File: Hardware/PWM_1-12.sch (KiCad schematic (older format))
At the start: 6 parts, among them J1 GH-6, J2 GH-6, J3 GH-6, J4 GH-6, J5 GH-6, J6 GH-6

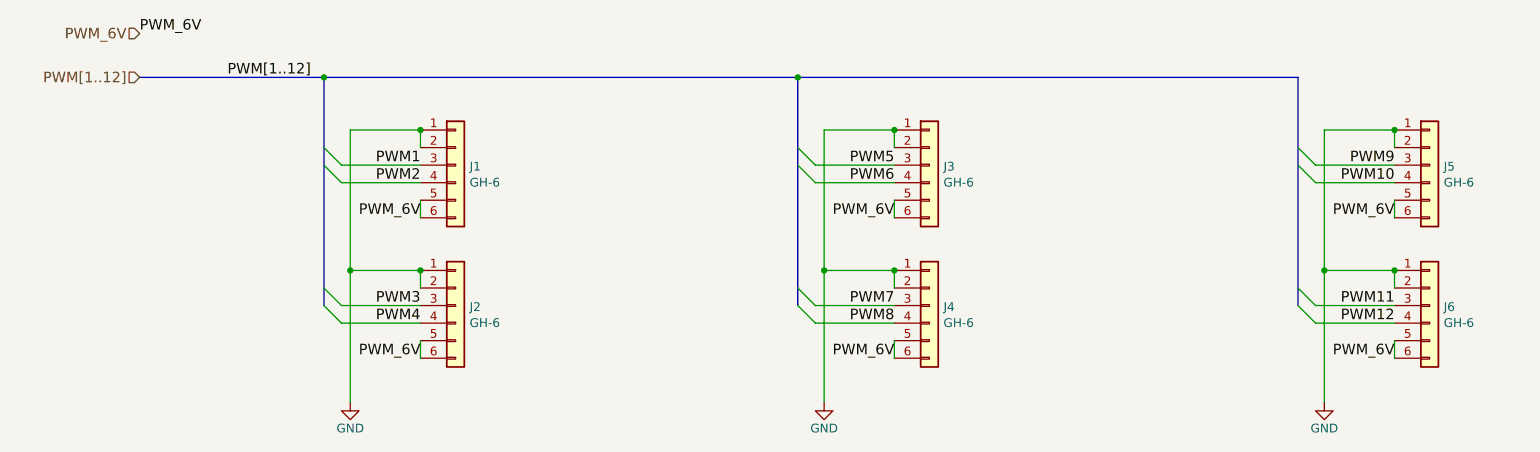
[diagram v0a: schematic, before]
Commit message: Added additional headers to some interfaces, GPIOs, and FTDI pins. Added silks
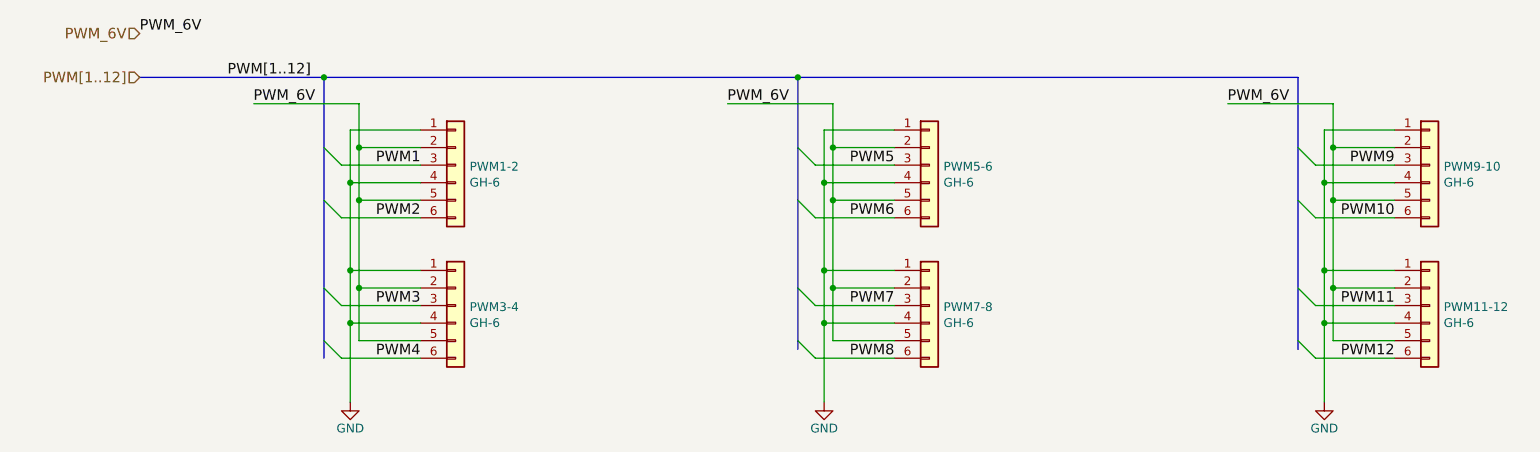
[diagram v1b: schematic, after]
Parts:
- PWM1-2: renamed from J1; part_num CONN-09 -> CONN-009
- PWM11-12: renamed from J6; part_num CONN-09 -> CONN-009
- PWM3-4: renamed from J2; part_num CONN-09 -> CONN-009
- PWM5-6: renamed from J3; part_num CONN-09 -> CONN-009
- PWM7-8: renamed from J4; part_num CONN-09 -> CONN-009
- PWM9-10: renamed from J5; part_num CONN-09 -> CONN-009
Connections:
- wire segments 36 -> 63
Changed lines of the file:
@@
 Text Label 2700 1400 2    60   ~ 0
 PWM1
-Text Label 2700 1500 2    60   ~ 0
+Text Label 2700 1700 2    60   ~ 0
 PWM2
 Text Label 2700 2200 2    60   ~ 0
 PWM3
-Text Label 2700 2300 2    60   ~ 0
+Text Label 2700 2500 2    60   ~ 0
 PWM4
 Text HLabel 1100 900  0    60   Input ~ 0
@@
 Text Label 1600 900  0    60   ~ 0
 PWM[1..12]
-Text Label 2700 2500 2    60   ~ 0
-PWM_6V
 Text Label 1100 650  0    60   ~ 0
-PWM_6V
-Text Label 2700 1700 2    60   ~ 0
 PWM_6V
 $Comp
@@
 $EndComp
 Entry Wire Line
-	2150 1400 2250 1500
+	2150 1600 2250 1700
 Entry Wire Line
 	2150 1300 2250 1400
 Wire Wire Line
-	2700 1500 2250 1500
+	2700 1700 2250 1700
 Wire Wire Line
 	2700 1400 2250 1400
-Wire Wire Line
-	2700 2000 2700 2100
 Entry Wire Line
 	2150 2100 2250 2200
 Entry Wire Line
-	2150 2200 2250 2300
+	2150 2400 2250 2500
 Wire Wire Line
 	2700 2200 2250 2200
 Wire Wire Line
-	2250 2300 2700 2300
+	2250 2500 2700 2500
 Wire Bus Line
 	1100 900  2150 900
@@
 Text Label 5400 1400 2    60   ~ 0
 PWM5
-Text Label 5400 1500 2    60   ~ 0
+Text Label 5400 1700 2    60   ~ 0
 PWM6
 Text Label 5400 2200 2    60   ~ 0
 PWM7
-Text Label 5400 2300 2    60   ~ 0
+Text Label 5400 2500 2    60   ~ 0
 PWM8
-Text Label 5400 1700 2    60   ~ 0
-PWM_6V
-Text Label 5400 2500 2    60   ~ 0
+Text Label 4800 1050 2    60   ~ 0
 PWM_6V
 $Comp
@@
 	1    0    0    -1
 $EndComp
-Wire Wire Line
-	5400 1200 5400 1300
-Wire Wire Line
-	5400 1700 5400 1600
-Entry Wire Line
-	4850 1400 4950 1500
+Entry Wire Line
+	4850 1600 4950 1700
 Entry Wire Line
 	4850 1300 4950 1400
 Wire Wire Line
-	5400 1500 4950 1500
+	5400 1700 4950 1700
 Wire Wire Line
 	5400 1400 4950 1400
 $Comp
-L Connector_Generic:Conn_01x06 J4
+L Connector_Generic:Conn_01x06 PWM7-8
 U 1 1 5CBF3F45
 P 5600 2200
-F 0 "J4" H 5680 2192 50  0000 L CNN
+F 0 "PWM7-8" H 5680 2192 50  0000 L CNN
 F 1 "GH-6" H 5680 2101 50  0000 L CNN
 F 2 "Connector_PinHeader_2.54mm:PinHeader_1x06_P2.54mm_Vertical" H 5600 2200 50  0001 C CNN
 F 3 "http://www.jst-mfg.com/product/pdf/eng/eGH.pdf" H 5600 2200 50  0001 C CNN
-F 4 "CONN-09" H 0   0   50  0001 C CNN "part_num"
+F 4 "CONN-009" H 0   0   50  0001 C CNN "part_num"
 	1    5600 2200
 	1    0    0    -1
 $EndComp
-Wire Wire Line
-	5400 2000 5400 2100
-Wire Wire Line
-	5400 2500 5400 2400
 Entry Wire Line
 	4850 2100 4950 2200
 Entry Wire Line
-	4850 2200 4950 2300
+	4850 2400 4950 2500
 Wire Wire Line
 	5400 2200 4950 2200
 Wire Wire Line
-	4950 2300 5400 2300
+	4950 2500 5400 2500
 Text Label 8250 1400 2    60   ~ 0
 PWM9
-Text Label 8250 1500 2    60   ~ 0
+Text Label 8250 1700 2    60   ~ 0
 PWM10
 Text Label 8250 2200 2    60   ~ 0
 PWM11
-Text Label 8250 2300 2    60   ~ 0
+Text Label 8250 2500 2    60   ~ 0
 PWM12
-Text Label 8250 2500 2    60   ~ 0
-PWM_6V
-Text Label 8250 1700 2    60   ~ 0
+Text Label 7650 1050 2    60   ~ 0
 PWM_6V
 $Comp
@@
 	1    0    0    -1
 $EndComp
-Wire Wire Line
-	8250 1200 8250 1300
-Wire Wire Line
-	8250 1700 8250 1600
-Entry Wire Line
-	7700 1400 7800 1500
+Entry Wire Line
+	7700 1600 7800 1700
 Entry Wire Line
 	7700 1300 7800 1400
 Wire Wire Line
-	8250 1500 7800 1500
+	8250 1700 7800 1700
 Wire Wire Line
 	8250 1400 7800 1400
-Wire Wire Line
-	8250 2000 8250 2100
-Wire Wire Line
-	8250 2500 8250 2400
 Entry Wire Line
 	7700 2100 7800 2200
 Entry Wire Line
-	7700 2200 7800 2300
+	7700 2400 7800 2500
 Wire Wire Line
 	8250 2200 7800 2200
 Wire Wire Line
-	7800 2300 8250 2300
+	7800 2500 8250 2500
 Connection ~ 4850 900
 Wire Bus Line
 	4850 900  7700 900
-Wire Wire Line
-	2700 2500 2700 2400
 Wire Wire Line
 	2700 2000 2300 2000
 Connection ~ 2300 2000
 Wire Wire Line
-	2300 2000 2300 2750
+	2300 2000 2300 2300
 Wire Wire Line
 	2300 1200 2700 1200
 Wire Wire Line
-	2300 1200 2300 2000
-Wire Wire Line
-	2700 1300 2700 1200
-Wire Wire Line
-	2700 1700 2700 1600
+	2300 1200 2300 1500
 Wire Wire Line
 	5000 1200 5400 1200
 Wire Wire Line
-	5000 1200 5000 2000
+	5000 1200 5000 1500
 Wire Wire Line
 	5400 2000 5000 2000
-Connection ~ 5400 2000
 Connection ~ 5000 2000
 Wire Wire Line
-	5000 2000 5000 2750
+	5000 2000 5000 2300
 Wire Wire Line
 	7850 1200 8250 1200
 Wire Wire Line
-	7850 1200 7850 2000
+	7850 1200 7850 1500
 Wire Wire Line
 	8250 2000 7850 2000
 Connection ~ 7850 2000
 Wire Wire Line
-	7850 2000 7850 2750
-$Comp
-L Connector_Generic:Conn_01x06 J3
+	7850 2000 7850 2300
+$Comp
+L Connector_Generic:Conn_01x06 PWM5-6
 U 1 1 5CEE26FD
 P 5600 1400
-F 0 "J3" H 5680 1392 50  0000 L CNN
+F 0 "PWM5-6" H 5680 1392 50  0000 L CNN
 F 1 "GH-6" H 5680 1301 50  0000 L CNN
 F 2 "Connector_PinHeader_2.54mm:PinHeader_1x06_P2.54mm_Vertical" H 5600 1400 50  0001 C CNN
 F 3 "http://www.jst-mfg.com/product/pdf/eng/eGH.pdf" H 5600 1400 50  0001 C CNN
-F 4 "CONN-09" H 0   -800 50  0001 C CNN "part_num"
+F 4 "CONN-009" H 0   -800 50  0001 C CNN "part_num"
 	1    5600 1400
 	1    0    0    -1
 $EndComp
-Connection ~ 5400 1200
-$Comp
-L Connector_Generic:Conn_01x06 J5
+$Comp
+L Connector_Generic:Conn_01x06 PWM9-10
 U 1 1 5CEE30E6
 P 8450 1400
-F 0 "J5" H 8530 1392 50  0000 L CNN
+F 0 "PWM9-10" H 8530 1392 50  0000 L CNN
 F 1 "GH-6" H 8530 1301 50  0000 L CNN
 F 2 "Connector_PinHeader_2.54mm:PinHeader_1x06_P2.54mm_Vertical" H 8450 1400 50  0001 C CNN
 F 3 "http://www.jst-mfg.com/product/pdf/eng/eGH.pdf" H 8450 1400 50  0001 C CNN
-F 4 "CONN-09" H 2850 -800 50  0001 C CNN "part_num"
+F 4 "CONN-009" H 2850 -800 50  0001 C CNN "part_num"
 	1    8450 1400
 	1    0    0    -1
 $EndComp
-Connection ~ 8250 1200
-$Comp
-L Connector_Generic:Conn_01x06 J6
+$Comp
+L Connector_Generic:Conn_01x06 PWM11-12
 U 1 1 5CEE3EBF
 P 8450 2200
-F 0 "J6" H 8530 2192 50  0000 L CNN
+F 0 "PWM11-12" H 8530 2192 50  0000 L CNN
 F 1 "GH-6" H 8530 2101 50  0000 L CNN
 F 2 "Connector_PinHeader_2.54mm:PinHeader_1x06_P2.54mm_Vertical" H 8450 2200 50  0001 C CNN
 F 3 "http://www.jst-mfg.com/product/pdf/eng/eGH.pdf" H 8450 2200 50  0001 C CNN
-F 4 "CONN-09" H 2850 0   50  0001 C CNN "part_num"
+F 4 "CONN-009" H 2850 0   50  0001 C CNN "part_num"
 	1    8450 2200
 	1    0    0    -1
 $EndComp
-Connection ~ 8250 2000
-$Comp
-L Connector_Generic:Conn_01x06 J2
+$Comp
+L Connector_Generic:Conn_01x06 PWM3-4
 U 1 1 5CEE43E8
 P 2900 2200
-F 0 "J2" H 2980 2192 50  0000 L CNN
+F 0 "PWM3-4" H 2980 2192 50  0000 L CNN
 F 1 "GH-6" H 2980 2101 50  0000 L CNN
 F 2 "Connector_PinHeader_2.54mm:PinHeader_1x06_P2.54mm_Vertical" H 2900 2200 50  0001 C CNN
 F 3 "http://www.jst-mfg.com/product/pdf/eng/eGH.pdf" H 2900 2200 50  0001 C CNN
-F 4 "CONN-09" H -2700 0   50  0001 C CNN "part_num"
+F 4 "CONN-009" H -2700 0   50  0001 C CNN "part_num"
 	1    2900 2200
 	1    0    0    -1
 $EndComp
-Connection ~ 2700 2000
-$Comp
-L Connector_Generic:Conn_01x06 J1
+$Comp
+L Connector_Generic:Conn_01x06 PWM1-2
 U 1 1 5CEE50A1
 P 2900 1400
-F 0 "J1" H 2980 1392 50  0000 L CNN
+F 0 "PWM1-2" H 2980 1392 50  0000 L CNN
 F 1 "GH-6" H 2980 1301 50  0000 L CNN
 F 2 "Connector_PinHeader_2.54mm:PinHeader_1x06_P2.54mm_Vertical" H 2900 1400 50  0001 C CNN
 F 3 "http://www.jst-mfg.com/product/pdf/eng/eGH.pdf" H 2900 1400 50  0001 C CNN
-F 4 "CONN-09" H -2700 -800 50  0001 C CNN "part_num"
+F 4 "CONN-009" H -2700 -800 50  0001 C CNN "part_num"
 	1    2900 1400
 	1    0    0    -1
 $EndComp
-Connection ~ 2700 1200
-Wire Bus Line
-	2150 900  2150 2200
-Wire Bus Line
-	4850 900  4850 2200
-Wire Bus Line
-	7700 900  7700 2200
+Wire Wire Line
+	4450 1050 5050 1050
+Wire Wire Line
+	5400 1300 5050 1300
+Connection ~ 5050 1300
+Wire Wire Line
+	5050 1300 5050 1050
+Wire Wire Line
+	5050 1300 5050 1600
+Wire Wire Line
+	5400 1600 5050 1600
+Connection ~ 5050 1600
+Wire Wire Line
+	5050 2400 5400 2400
+Wire Wire Line
+	5050 1600 5050 2100
+Wire Wire Line
+	5400 2300 5000 2300
+Connection ~ 5000 2300
+Wire Wire Line
+	5000 2300 5000 2750
+Wire Wire Line
+	5400 1500 5000 1500
+Connection ~ 5000 1500
+Wire Wire Line
+	5000 1500 5000 2000
+Wire Wire Line
+	5400 2100 5050 2100
+Connection ~ 5050 2100
+Wire Wire Line
+	5050 2100 5050 2400
+Wire Wire Line
+	2700 1300 2350 1300
+Wire Wire Line
+	2350 1300 2350 1050
+Text Label 2100 1050 2    60   ~ 0
+PWM_6V
+Wire Wire Line
+	1750 1050 2350 1050
+Wire Wire Line
+	2350 1300 2350 1600
+Wire Wire Line
+	2350 1600 2700 1600
+Connection ~ 2350 1300
+Wire Wire Line
+	2350 1600 2350 2100
+Wire Wire Line
+	2350 2100 2700 2100
+Connection ~ 2350 1600
+Wire Wire Line
+	2350 2100 2350 2400
+Wire Wire Line
+	2350 2400 2700 2400
+Connection ~ 2350 2100
+Wire Wire Line
+	7900 1050 7300 1050
+Wire Wire Line
+	8250 1300 7900 1300
+Connection ~ 7900 1300
+Wire Wire Line
+	7900 1300 7900 1050
+Wire Wire Line
+	8250 2100 7900 2100
+Wire Wire Line
+	8250 2300 7850 2300
+Connection ~ 7850 2300
+Wire Wire Line
+	7850 2300 7850 2750
+Wire Wire Line
+	7900 2100 7900 2400
+Wire Wire Line
+	7900 2400 8250 2400
+Connection ~ 7900 2100
+Wire Wire Line
+	2700 2300 2300 2300
+Connection ~ 2300 2300
+Wire Wire Line
+	2300 2300 2300 2750
+Wire Wire Line
+	2700 1500 2300 1500
+Connection ~ 2300 1500
+Wire Wire Line
+	2300 1500 2300 2000
+Wire Wire Line
+	7900 1300 7900 1600
+Wire Wire Line
+	8250 1500 7850 1500
+Connection ~ 7850 1500
+Wire Wire Line
+	7850 1500 7850 2000
+Wire Wire Line
+	7900 1600 8250 1600
+Wire Bus Line
+	7700 900  7700 2450
+Wire Bus Line
+	4850 900  4850 2450
+Wire Bus Line
+	2150 900  2150 2500
+Connection ~ 7900 1600
+Wire Wire Line
+	7900 1600 7900 2100
 $EndSCHEMATC
